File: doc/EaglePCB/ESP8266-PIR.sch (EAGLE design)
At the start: 10 parts, among them IC2 DS1820, IC3 LM340S

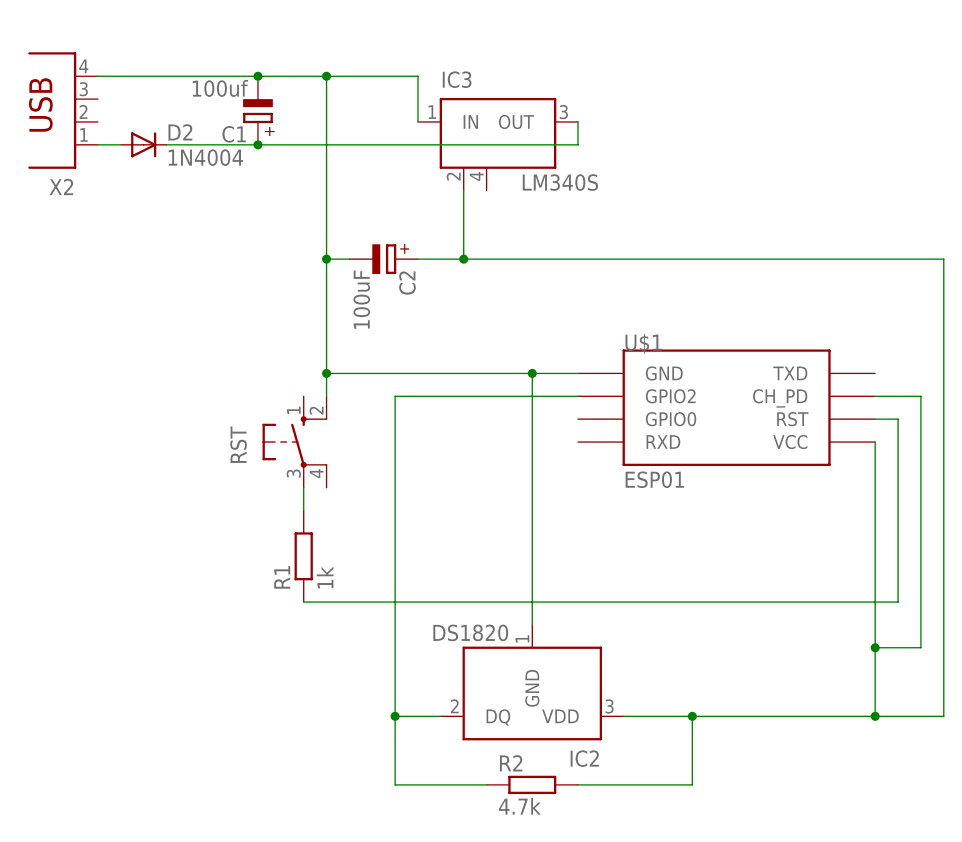
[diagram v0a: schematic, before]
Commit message: correct PCB design and add PIR IoT device
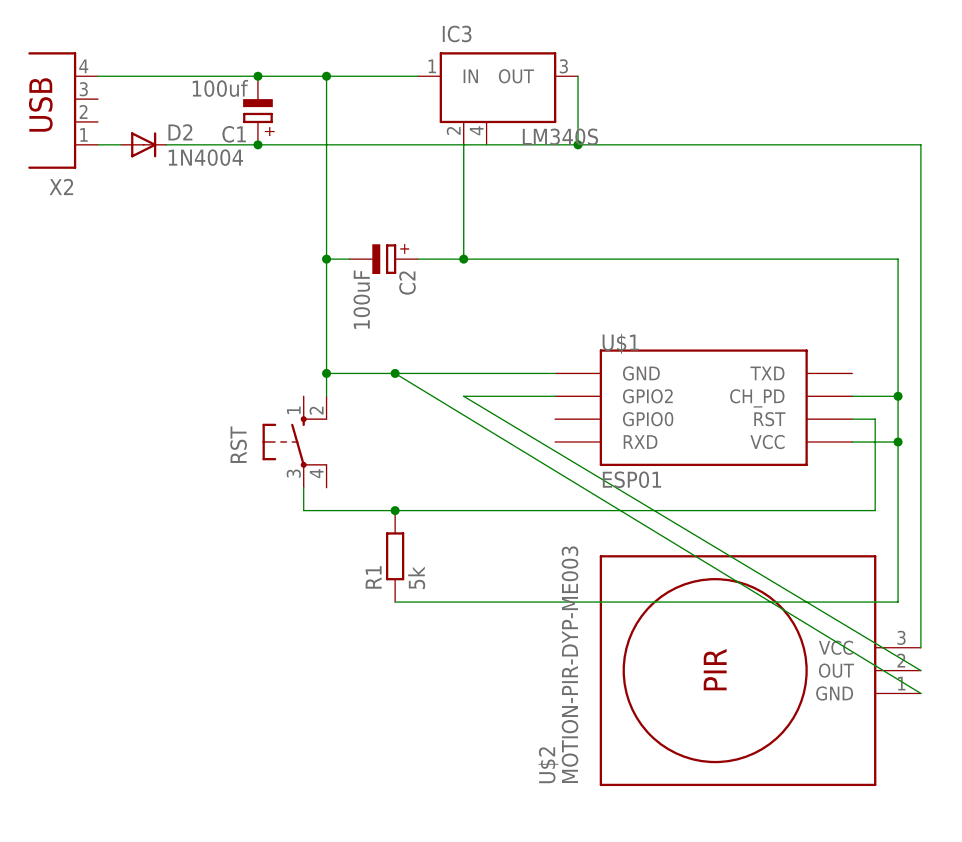
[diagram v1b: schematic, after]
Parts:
- removed IC2: DS1820, DS1820:DS1820
- removed R2: 4.7k, resistor:R-EU_0207/12
- added U$2: MOTION-PIR-DYP-ME003, diy-modules:MOTION-PIR-DYP-ME003
- R1: value 1k -> 5k; device resistor:R-EU_0207/12 -> eagle-ltspice:R0204/7
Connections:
- removed net DQ: IC2.DQ, R2.1, U$1.GPIO2
- removed net GND(RST): R1.2, RST.P
- removed net RST: R1.1, U$1.RST
- new net GPIO2: U$1.GPIO2, U$2.OUT
- new net N$4: R1.2, RST.P, U$1.RST
- net 3V3: now also R1.1; no longer IC2.VDD, R2.2
- net 5V: now also U$2.VCC
- net GND: now also U$2.GND; no longer IC2.GND
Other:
- moved on the sheet: IC3, R1, U$1
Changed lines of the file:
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@@
 <part name="X2" library="con-berg" deviceset="PN61729" device=""/>
 <part name="RST" library="switch-omron" deviceset="10-XX" device=""/>
-<part name="IC2" library="DS1820" deviceset="DS1820" device=""/>
 <part name="D2" library="diode" deviceset="1N4004" device=""/>
 <part name="C2" library="rcl" deviceset="CPOL-EU" device="E2.5-5" value="100uF"/>
-<part name="R1" library="resistor" deviceset="R-EU_" device="0207/12" value="1k"/>
-<part name="R2" library="resistor" deviceset="R-EU_" device="0207/12" value="4.7k"/>
 <part name="C1" library="rcl" deviceset="CPOL-EU" device="E2.5-5" value="100uf"/>
 <part name="IC3" library="linear" deviceset="LM340S" device=""/>
+<part name="U$2" library="diy-modules" deviceset="MOTION-PIR-DYP-ME003" device=""/>
+<part name="R1" library="eagle-ltspice" deviceset="R" device="0204/7" value="5k"/>
 </parts>
 <sheets>
@@
 </plain>
 <instances>
-<instance part="U$1" gate="G$1" x="55.88" y="48.26"/>
+<instance part="U$1" gate="G$1" x="53.34" y="48.26"/>
 <instance part="X2" gate="G$1" x="-17.78" y="86.36" rot="R180"/>
 <instance part="RST" gate="1" x="7.62" y="48.26"/>
-<instance part="IC2" gate="G$1" x="33.02" y="20.32" rot="R180"/>
 <instance part="D2" gate="1" x="-10.16" y="81.28"/>
 <instance part="C2" gate="G$1" x="17.78" y="68.58" rot="R270"/>
-<instance part="R1" gate="G$1" x="7.62" y="35.56" rot="R90"/>
-<instance part="R2" gate="G$1" x="33.02" y="10.16"/>
 <instance part="C1" gate="G$1" x="2.54" y="83.82" rot="R180"/>
-<instance part="IC3" gate="G$1" x="27.94" y="81.28"/>
+<instance part="IC3" gate="G$1" x="27.94" y="86.36"/>
+<instance part="U$2" gate="G$1" x="55.88" y="22.86" rot="R90"/>
+<instance part="R1" gate="G$1" x="17.78" y="35.56" rot="R90"/>
 </instances>
 <busses>
@@
 <pinref part="IC3" gate="G$1" pin="OUT"/>
 <wire x1="2.54" y1="81.28" x2="38.1" y2="81.28" width="0.1524" layer="91"/>
-<wire x1="38.1" y1="81.28" x2="38.1" y2="83.82" width="0.1524" layer="91"/>
+<wire x1="38.1" y1="81.28" x2="38.1" y2="88.9" width="0.1524" layer="91"/>
 <junction x="2.54" y="81.28"/>
+<junction x="38.1" y="81.28"/>
+<wire x1="38.1" y1="81.28" x2="76.2" y2="81.28" width="0.1524" layer="91"/>
+<wire x1="76.2" y1="81.28" x2="76.2" y2="25.4" width="0.1524" layer="91"/>
+<pinref part="U$2" gate="G$1" pin="VCC"/>
 </segment>
 <segment>
@@
 <wire x1="10.16" y1="55.88" x2="10.16" y2="68.58" width="0.1524" layer="91"/>
 <pinref part="U$1" gate="G$1" pin="GND"/>
-<wire x1="10.16" y1="55.88" x2="33.02" y2="55.88" width="0.1524" layer="91"/>
-<wire x1="33.02" y1="55.88" x2="38.1" y2="55.88" width="0.1524" layer="91"/>
-<junction x="33.02" y="55.88"/>
-<wire x1="33.02" y1="55.88" x2="33.02" y2="27.94" width="0.1524" layer="91"/>
-<pinref part="IC2" gate="G$1" pin="GND"/>
+<wire x1="10.16" y1="55.88" x2="17.78" y2="55.88" width="0.1524" layer="91"/>
+<wire x1="17.78" y1="55.88" x2="35.56" y2="55.88" width="0.1524" layer="91"/>
+<junction x="17.78" y="55.88"/>
+<wire x1="17.78" y1="55.88" x2="76.2" y2="20.32" width="0.1524" layer="91"/>
 <junction x="10.16" y="88.9"/>
 <pinref part="IC3" gate="G$1" pin="IN"/>
 <wire x1="10.16" y1="88.9" x2="20.32" y2="88.9" width="0.1524" layer="91"/>
-<wire x1="20.32" y1="88.9" x2="20.32" y2="83.82" width="0.1524" layer="91"/>
 <junction x="2.54" y="88.9"/>
+<pinref part="U$2" gate="G$1" pin="GND"/>
 </segment>
 </net>
@@
 <pinref part="C2" gate="G$1" pin="+"/>
 <pinref part="IC3" gate="G$1" pin="GND@1"/>
-<wire x1="25.4" y1="76.2" x2="25.4" y2="68.58" width="0.1524" layer="91"/>
+<wire x1="25.4" y1="81.28" x2="25.4" y2="68.58" width="0.1524" layer="91"/>
 <wire x1="25.4" y1="68.58" x2="20.32" y2="68.58" width="0.1524" layer="91"/>
 <junction x="25.4" y="68.58"/>
-<wire x1="25.4" y1="68.58" x2="78.74" y2="68.58" width="0.1524" layer="91"/>
-<wire x1="78.74" y1="68.58" x2="78.74" y2="17.78" width="0.1524" layer="91"/>
+<wire x1="25.4" y1="68.58" x2="73.66" y2="68.58" width="0.1524" layer="91"/>
+<wire x1="73.66" y1="68.58" x2="73.66" y2="53.34" width="0.1524" layer="91"/>
+<pinref part="U$1" gate="G$1" pin="CH_PD"/>
+<wire x1="73.66" y1="53.34" x2="68.58" y2="53.34" width="0.1524" layer="91"/>
+<junction x="73.66" y="53.34"/>
 <pinref part="U$1" gate="G$1" pin="VCC"/>
-<wire x1="71.12" y1="48.26" x2="71.12" y2="25.4" width="0.1524" layer="91"/>
-<pinref part="IC2" gate="G$1" pin="VDD"/>
-<wire x1="71.12" y1="25.4" x2="71.12" y2="17.78" width="0.1524" layer="91"/>
-<wire x1="71.12" y1="17.78" x2="50.8" y2="17.78" width="0.1524" layer="91"/>
-<wire x1="50.8" y1="17.78" x2="43.18" y2="17.78" width="0.1524" layer="91"/>
-<wire x1="50.8" y1="17.78" x2="50.8" y2="10.16" width="0.1524" layer="91"/>
-<pinref part="R2" gate="G$1" pin="2"/>
-<wire x1="50.8" y1="10.16" x2="38.1" y2="10.16" width="0.1524" layer="91"/>
-<junction x="71.12" y="17.78"/>
-<wire x1="78.74" y1="17.78" x2="71.12" y2="17.78" width="0.1524" layer="91"/>
-<junction x="50.8" y="17.78"/>
-<junction x="71.12" y="25.4"/>
-<pinref part="U$1" gate="G$1" pin="CH_PD"/>
-<wire x1="71.12" y1="53.34" x2="76.2" y2="53.34" width="0.1524" layer="91"/>
-<wire x1="76.2" y1="53.34" x2="76.2" y2="25.4" width="0.1524" layer="91"/>
-<wire x1="76.2" y1="25.4" x2="71.12" y2="25.4" width="0.1524" layer="91"/>
+<wire x1="68.58" y1="48.26" x2="73.66" y2="48.26" width="0.1524" layer="91"/>
+<wire x1="73.66" y1="48.26" x2="73.66" y2="53.34" width="0.1524" layer="91"/>
+<pinref part="R1" gate="G$1" pin="1"/>
+<wire x1="17.78" y1="30.48" x2="73.66" y2="30.48" width="0.1524" layer="91"/>
+<wire x1="73.66" y1="30.48" x2="73.66" y2="48.26" width="0.1524" layer="91"/>
+<junction x="73.66" y="48.26"/>
 </segment>
 </net>
-<net name="RST" class="0">
+<net name="GPIO2" class="0">
 <segment>
-<pinref part="R1" gate="G$1" pin="1"/>
-<wire x1="7.62" y1="30.48" x2="73.66" y2="30.48" width="0.1524" layer="91"/>
-<wire x1="73.66" y1="30.48" x2="73.66" y2="50.8" width="0.1524" layer="91"/>
-<pinref part="U$1" gate="G$1" pin="RST"/>
-<wire x1="73.66" y1="50.8" x2="71.12" y2="50.8" width="0.1524" layer="91"/>
+<pinref part="U$1" gate="G$1" pin="GPIO2"/>
+<pinref part="U$2" gate="G$1" pin="OUT"/>
+<wire x1="35.56" y1="53.34" x2="25.4" y2="53.34" width="0.1524" layer="91"/>
+<wire x1="25.4" y1="53.34" x2="76.2" y2="22.86" width="0.1524" layer="91"/>
 </segment>
 </net>
-<net name="DQ" class="0">
+<net name="N$4" class="0">
 <segment>
-<pinref part="R2" gate="G$1" pin="1"/>
-<wire x1="27.94" y1="10.16" x2="17.78" y2="10.16" width="0.1524" layer="91"/>
-<wire x1="17.78" y1="10.16" x2="17.78" y2="17.78" width="0.1524" layer="91"/>
-<pinref part="IC2" gate="G$1" pin="DQ"/>
-<wire x1="17.78" y1="17.78" x2="22.86" y2="17.78" width="0.1524" layer="91"/>
-<junction x="17.78" y="17.78"/>
-<wire x1="17.78" y1="17.78" x2="17.78" y2="53.34" width="0.1524" layer="91"/>
-<pinref part="U$1" gate="G$1" pin="GPIO2"/>
-<wire x1="17.78" y1="53.34" x2="38.1" y2="53.34" width="0.1524" layer="91"/>
+<pinref part="U$1" gate="G$1" pin="RST"/>
+<wire x1="68.58" y1="50.8" x2="71.12" y2="50.8" width="0.1524" layer="91"/>
+<wire x1="71.12" y1="50.8" x2="71.12" y2="40.64" width="0.1524" layer="91"/>
+<wire x1="71.12" y1="40.64" x2="17.78" y2="40.64" width="0.1524" layer="91"/>
+<pinref part="RST" gate="1" pin="P"/>
+<wire x1="17.78" y1="40.64" x2="7.62" y2="40.64" width="0.1524" layer="91"/>
+<wire x1="7.62" y1="40.64" x2="7.62" y2="43.18" width="0.1524" layer="91"/>
+<pinref part="R1" gate="G$1" pin="2"/>
+<junction x="17.78" y="40.64"/>
 </segment>
 </net>
-<net name="GND(RST)" class="0">
-<segment>
-<pinref part="RST" gate="1" pin="P"/>
-<pinref part="R1" gate="G$1" pin="2"/>
-<wire x1="7.62" y1="40.64" x2="7.62" y2="43.18" width="0.1524" layer="91"/>
-</segment>
-</net>
